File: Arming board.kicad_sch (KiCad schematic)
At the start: 11 parts, among them J2 Conn_01x01_Pin, J3 Conn_01x01_Pin, J4 Conn_01x04_Pin, Q1 SQS141ELNW-T1_GE3

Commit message: Add files via upload
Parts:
- added F2: 50m, Fuse:Fuse_Bourns_TBU-CA, symbol Power_Protection:TBU-CA040-200-WH
- added Q2: SQS141ELNW-T1_GE3, eigene:POWERPAK-1212-8, symbol SQS141ELNW-T1_GE3:SQS141ELNW-T1_GE3
- D2: footprint (none) -> LED_SMD:LED_0603_1608Metric
- DZ1, DZ2, DZ3: footprint (none) -> Diode_SMD:D_SOD-123
- F1: value TBU-CA040-200-WH -> 50m
- J2, J3: footprint (none) -> Connector_PinHeader_1.00mm:PinHeader_1x01_P1.00mm_Horizontal
- J4: footprint (none) -> Connector_PinHeader_1.00mm:PinHeader_1x04_P1.00mm_Horizontal
- R10, R9: value R -> 4.7k; footprint (none) -> Resistor_SMD:R_0805_2012Metric
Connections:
- net BATT_armed: now also Q2.5, Q2.6, Q2.7, Q2.8, Q2.9
- net +BATT renamed Batt+
- net Batt+: now also F2.3, Q2.1, Q2.2, Q2.3
- net Arming logic 1/power_fused renamed Arming logic 1/pwr_fused
- net Disarm renamed Disarm_In_1
- new net Arming logic 2/out: Q2.4
- new net Arming logic 2/pwr_fused: F2.1
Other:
- added sheet Arming logic 2 (Arming logic.kicad_sch)
- sheet Arming logic 1 ports: added arm, disarm, pwr_fused; removed Arm, Disarm, power_fused
- moved on the sheet: D2, DZ1, DZ2, DZ3, R10, R9

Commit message: Add files via upload
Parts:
- removed F2: 50m, Fuse:Fuse_Bourns_TBU-CA, symbol Power_Protection:TBU-CA040-200-WH
- removed J4: Conn_01x04_Pin, Connector_PinHeader_1.00mm:PinHeader_1x04_P1.00mm_Horizontal, symbol Connector:Conn_01x04_Pin
- added D4: 16V, symbol Device:D
- added F2: 50m, symbol Device:Fuse
- added J1: Conn_01x04_Pin, symbol Connector:Conn_01x04_Pin
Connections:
- net Arm_In_1: now also J1.1 (Pin_1)
- net Arming logic 2/pwr_fused: now also F2.2
- net BATT_armed: now also D4.1 (K)
- net Batt+: no longer F1.3, Q1.1, Q1.2, Q1.3, Q2.1, Q2.2, Q2.3
- net Disarm_In_1: now also J1.4 (Pin_4)
- net GND: now also D4.2 (A), J1.2 (Pin_2), J1.3 (Pin_3)
- new net VCC: F1.3, F2.1, Q1.1, Q1.2, Q1.3, Q2.1, Q2.2, Q2.3
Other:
- moved on the sheet: D2, DZ1, DZ2, DZ3, R10, R9

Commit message: Add files via upload
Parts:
- D4: footprint (none) -> Diode_SMD:D_SOD-123
- F2: footprint (none) -> Fuse:Fuse_Bourns_TBU-CA
- J1: footprint (none) -> Connector_PinHeader_1.00mm:PinHeader_1x04_P1.00mm_Horizontal
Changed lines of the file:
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@@
 			)
 		)
-		(property "Footprint" ""
+		(property "Footprint" "Connector_PinHeader_1.00mm:PinHeader_1x04_P1.00mm_Horizontal"
 			(at 41.91 96.52 0)
 			(effects
@@
 			)
 		)
-		(property "Footprint" ""
+		(property "Footprint" "Fuse:Fuse_Bourns_TBU-CA"
 			(at 167.132 34.29 90)
 			(effects
@@
 			)
 		)
-		(property "Footprint" ""
+		(property "Footprint" "Diode_SMD:D_SOD-123"
 			(at 100.33 107.95 0)
 			(effects

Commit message: continued scematic
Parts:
- removed J1: Conn_01x04_Pin, Connector_PinHeader_1.00mm:PinHeader_1x04_P1.00mm_Horizontal, symbol Connector:Conn_01x04_Pin
- removed J2, J3: Conn_01x01_Pin, Connector_PinHeader_1.00mm:PinHeader_1x01_P1.00mm_Horizontal, symbol Connector:Conn_01x01_Pin
- added IC1: CD4043BDR, SOIC127P600X175-16N, symbol rapid_arming:CD4043BDR
- added J1, J11, J4: ~, stigma:Molex_Micro-Fit_3.0_43045-0400_2x02_P3.00mm_Horizontal, symbol Connector_Generic:Conn_02x02_Top_Bottom
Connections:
- net Arm_In_1: no longer DZ1.1 (K)
- net BATT_armed: no longer D4.1 (K), Q1.5, Q1.6, Q1.7, Q1.8, Q1.9, Q2.5, Q2.6, Q2.7, Q2.8, Q2.9
- net GND: now also IC1.8 (VSS), J1.1 (Pin_1), J1.2 (Pin_2), J11.1 (Pin_1), J11.2 (Pin_2), J4.1 (Pin_1), J4.2 (Pin_2)
- net VCC: now also IC1.16 (VDD); no longer Q1.1, Q1.2, Q1.3, Q2.1, Q2.2, Q2.3
- net Arming logic 1/out: no longer names the net of Q1.4
- net Arming logic 1/pwr_fused: no longer names the net of F1.1
- net Arming logic 2/out: no longer names the net of Q2.4
- net Arming logic 2/pwr_fused: no longer names the net of F2.2
- net Batt+ renamed +BATT
- net +BATT: now also Q1.1, Q1.2, Q1.3, Q2.1, Q2.2, Q2.3, J1.3 (Pin_3), J1.4 (Pin_4)
- net Disarm_In_1 renamed disarm
- net disarm: now also IC1.3 (R1), IC1.7 (R2), J11.4 (Pin_4)
- new net +BATT_ARM: D4.1 (K), J4.3 (Pin_3), J4.4 (Pin_4), Q1.5, Q1.6, Q1.7, Q1.8, Q1.9, Q2.5, Q2.6, Q2.7, Q2.8, Q2.9
- new net arm: DZ1.1 (K), IC1.4 (S1), IC1.6 (S2), J11.3 (Pin_3)
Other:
- removed sheet Arming logic 1
- removed sheet Arming logic 2
- note added: "Power In"
- note added: "Power Out"
- note added: "arm/disarm conn."
- moved on the sheet: D2, D4, DZ1, DZ2, DZ3, F1, F2, Q1, Q2, R10, R9

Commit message: continued schematic
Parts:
- removed DZ1, DZ2, DZ3: 16V, Diode_SMD:D_SOD-123, symbol PCM_Diode_Zener_AKL:D_Zener_Generic
- removed F1: 50m, Fuse:Fuse_Bourns_TBU-CA, symbol Power_Protection:TBU-CA040-200-WH
- removed F2: 50m, Fuse:Fuse_Bourns_TBU-CA, symbol Device:Fuse
- removed J11, J4: ~, stigma:Molex_Micro-Fit_3.0_43045-0400_2x02_P3.00mm_Horizontal, symbol Connector_Generic:Conn_02x02_Top_Bottom
- removed Q2: SQS141ELNW-T1_GE3, eigene:POWERPAK-1212-8, symbol SQS141ELNW-T1_GE3:SQS141ELNW-T1_GE3
- added C1, C2: C, Capacitor_SMD:C_0402_1005Metric, symbol Device:C
- added D1, D3, D5: ESD5Zxx, Diode_SMD:D_SOD-523, symbol Diode:ESD5Zxx
- added J2: ~, stigma:Molex_Micro-Fit_3.0_43045-0400_2x02_P3.00mm_Horizontal, symbol Connector_Generic:Conn_02x02_Top_Bottom
- added J3: Conn_02x03_Counter_Clockwise, symbol Connector_Generic:Conn_02x03_Counter_Clockwise
- added R1, R5: 10k, Resistor_SMD:R_0402_1005Metric_Pad0.72x0.64mm_HandSolder, symbol Device:R
- added R2: 1k, symbol Device:R
- added R3, R4: R, Resistor_SMD:R_0402_1005Metric, symbol Device:R
- IC1: LCSC (none) -> C40131
- Q1: Availability In Stock -> (none); Check_prices https://www.snapeda.com/parts/SQS141ELNW-T1/GE3/Vishay/view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 -> (none); Description_1 MOSFET, P-CH/40V/101A/POWERPAK 1212-8SLW ROHS COMPLIANT: YES -> 55℃~+175℃ 1 P-Channel 10mΩ@10V 119W 141nC@10V 2V 347pF 40V 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; LCSC (none) -> C6818689; MP SQS141ELNW-T1/GE3 -> (none); Package None -> (none); Price None -> (none); SnapEDA_Link https://www.snapeda.com/parts/SQS141ELNW-T1/GE3/Vishay/view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 -> (none)
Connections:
- net +BATT: now also D5.1 (K)
- net +BATT_ARM: now also J2.3 (Pin_3), J2.4 (Pin_4)
- net GND: now also C1.2, C2.2, D1.2 (A), D3.2 (A), D5.2 (A), J2.1 (Pin_1), J2.2 (Pin_2), J3.1 (Pin_1)
- net VCC: now also J3.6 (Pin_6), R1.2, R5.2
- net arm: now also IC1.7 (R2), C1.1, R3.2; no longer IC1.4 (S1), IC1.6 (S2)
- net disarm: now also IC1.6 (S2), C2.1, R4.2; no longer IC1.3 (R1), IC1.7 (R2)
- net at Q1.4: now also R1.1, R2.2
- net at IC1.5 (ENABLE): now also R5.1
- net at IC1.9 (Q2): now also R2.1
- new net: D3.1 (K), J3.4 (Pin_4), R4.1
- new net: D1.1 (K), J3.5 (Pin_5), R3.1
- no-connect marks 0 -> 9
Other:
- note added: "flyback"
- note added: "gate current limit resistor?"
- moved on the sheet: D2, D4, IC1, Q1, R10, R9

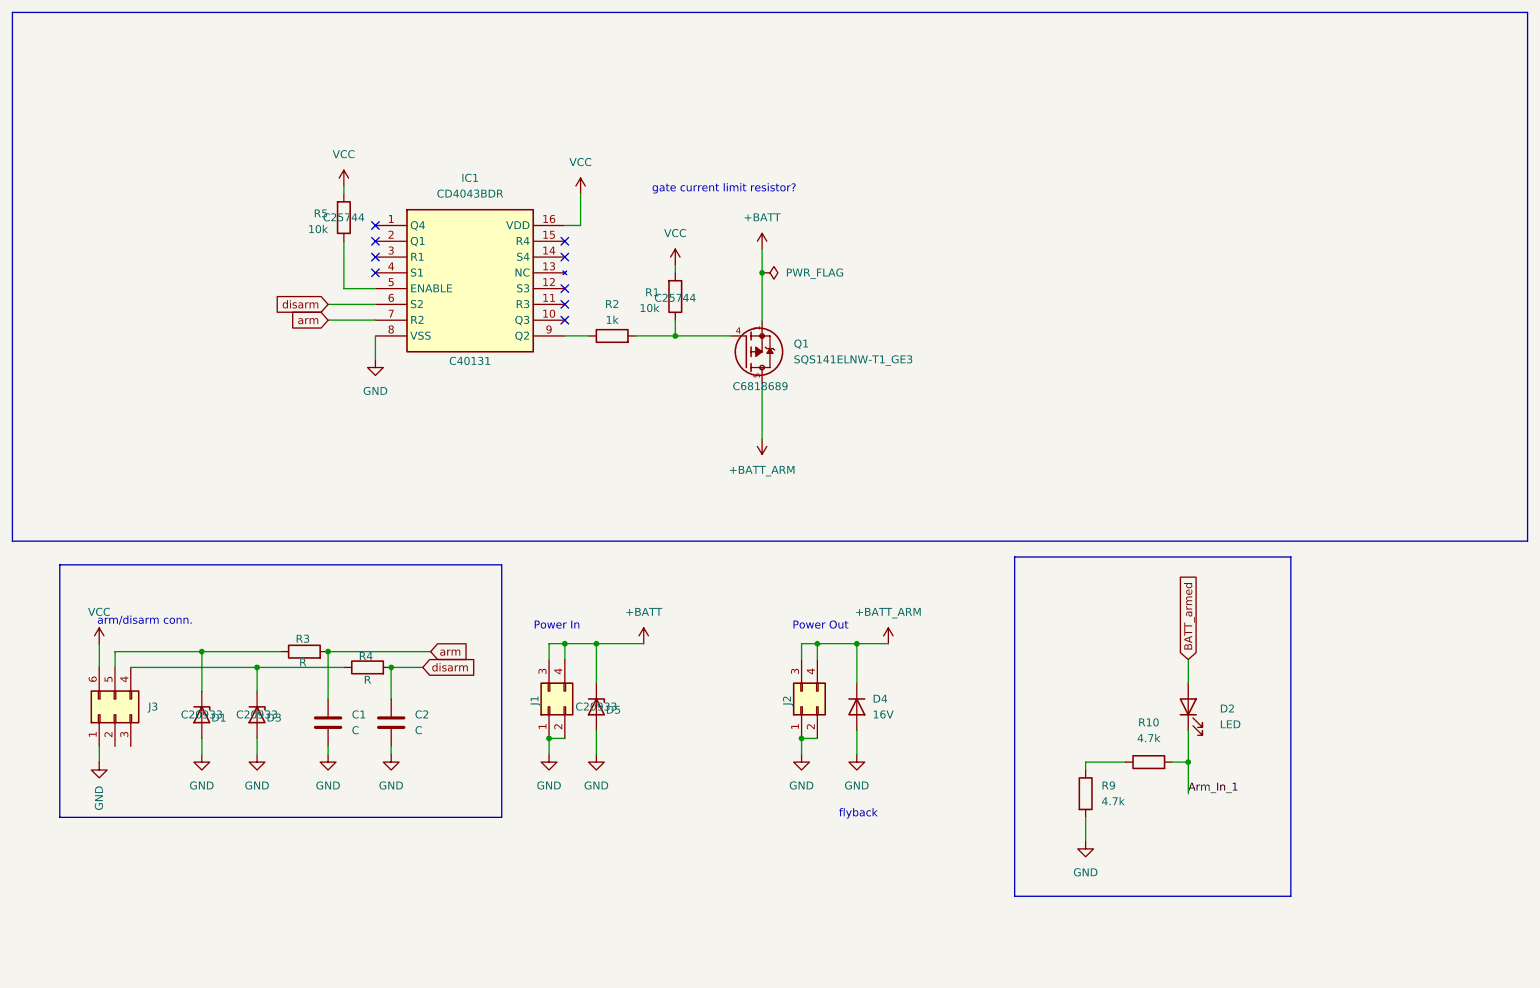
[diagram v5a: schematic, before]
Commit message: finished first scematic draft
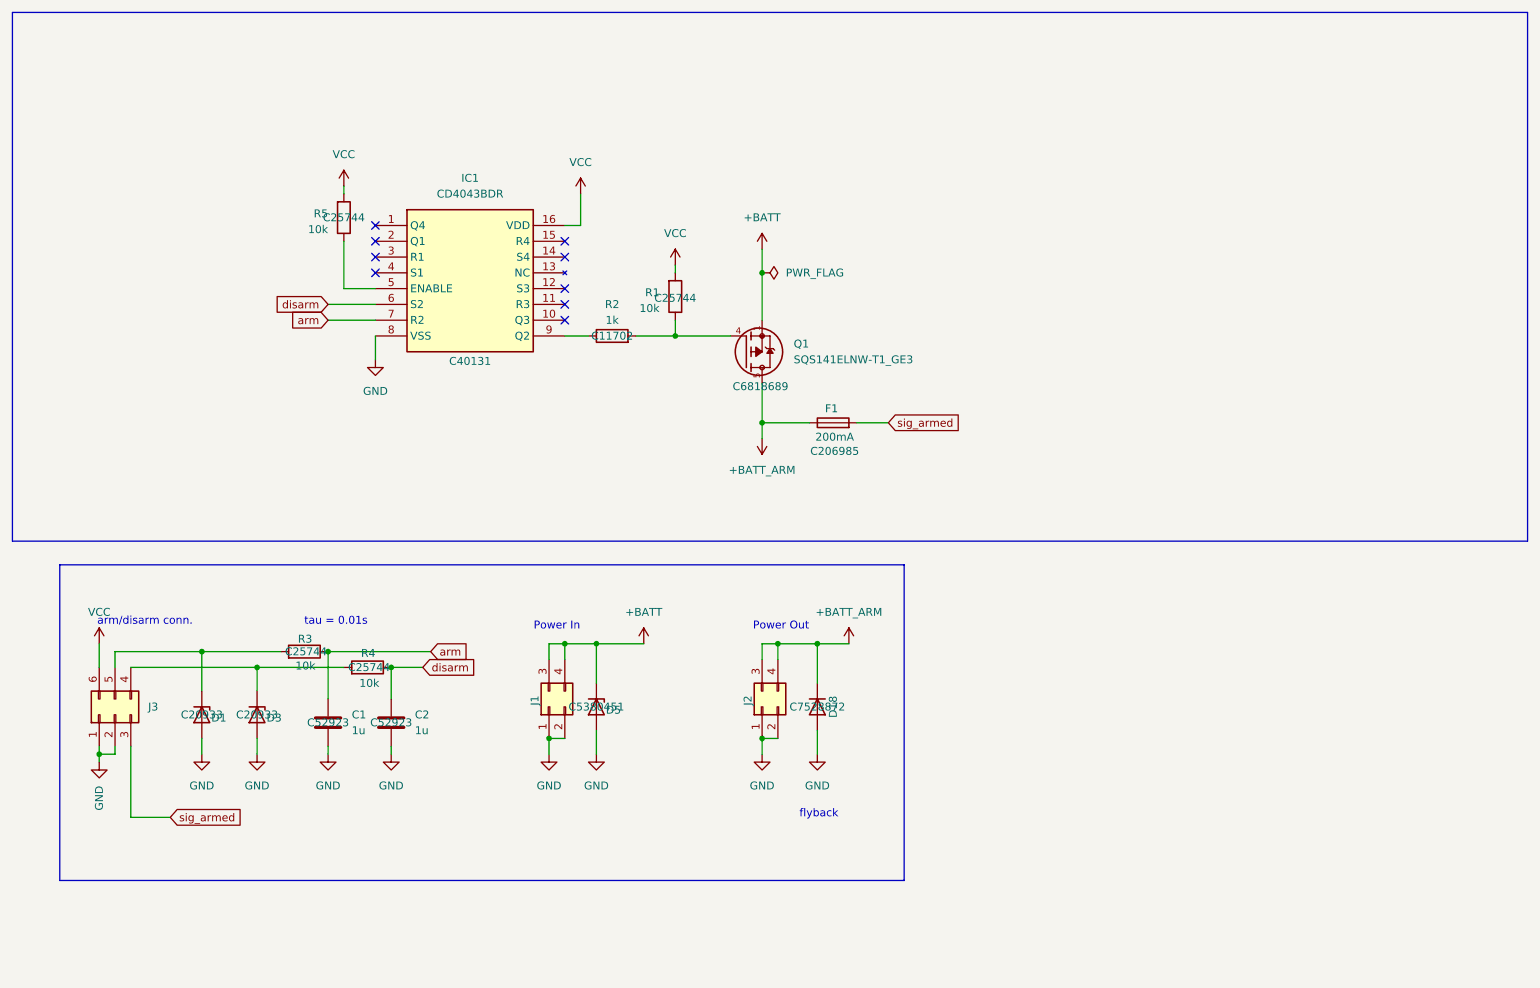
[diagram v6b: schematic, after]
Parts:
- removed D2: LED, LED_SMD:LED_0603_1608Metric, symbol Device:LED
- removed D4: 16V, Diode_SMD:D_SOD-123, symbol Device:D
- removed R10, R9: 4.7k, Resistor_SMD:R_0805_2012Metric, symbol Device:R
- added D18: D, Diode_SMD:D_SOD-323_HandSoldering, symbol Device:D
- added F1: 200mA, Fuse:Fuse_1206_3216Metric_Pad1.42x1.75mm_HandSolder, symbol Device:Fuse
- C1, C2: value C -> 1u; LCSC (none) -> C52923
- D5: value ESD5Zxx -> TS1811LD-CX; LCSC C20933 -> C5380451
- J1, J2: footprint stigma:Molex_Micro-Fit_3.0_43045-0400_2x02_P3.00mm_Horizontal -> Connector_Molex:Molex_Micro-Fit_3.0_43045-0400_2x02_P3.00mm_Horizontal
- J3: footprint (none) -> Connector_Molex:Molex_Micro-Fit_3.0_43045-0600_2x03_P3.00mm_Horizontal
- Q1: footprint eigene:POWERPAK-1212-8 -> rapid_arming:POWERPAK-1212-8
- R2: footprint (none) -> Resistor_SMD:R_0402_1005Metric_Pad0.72x0.64mm_HandSolder; LCSC (none) -> C11702
- R3, R4: value R -> 10k; footprint Resistor_SMD:R_0402_1005Metric -> Resistor_SMD:R_0402_1005Metric_Pad0.72x0.64mm_HandSolder; LCSC (none) -> C25744
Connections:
- net +BATT_ARM: now also D18.1 (K), F1.1
- net GND: now also J3.2 (Pin_2), D18.2 (A)
- net arm: now also R3.1; no longer R3.2
- net disarm: now also R4.1; no longer R4.2
- net sig_armed: now reaches J3.3 (Pin_3)
- net sig_armed: now also F1.2
- net at D3.1 (K), J3.4 (Pin_4): now also R4.2; no longer R4.1
- net at D1.1 (K), J3.5 (Pin_5): now also R3.2; no longer R3.1
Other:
- note added: "tau = 0.01s"
- note removed: "gate current limit resistor?"
- moved on the sheet: J2

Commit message: Replaced 6-Pin with 4-Pin connector, added input pulldown
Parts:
- removed F1: 200mA, Fuse:Fuse_1206_3216Metric_Pad1.42x1.75mm_HandSolder, symbol Device:Fuse
- removed J3: Conn_02x03_Counter_Clockwise, Connector_Molex:Molex_Micro-Fit_3.0_43045-0600_2x03_P3.00mm_Horizontal, symbol Connector_Generic:Conn_02x03_Counter_Clockwise
- added D19: D, Diode_SMD:D_SOD-323_HandSoldering, symbol Device:D
- added D6: TS1811LD-CX, Diode_SMD:D_SOD-523, symbol Diode:ESD5Zxx
- added J4, J5, J6: (no value), Connector_Molex:Molex_Micro-Fit_3.0_43045-0400_2x02_P3.00mm_Horizontal, symbol Connector_Generic:Conn_02x02_Top_Bottom
- added R6, R7: 10k, Resistor_SMD:R_0402_1005Metric_Pad0.72x0.64mm_HandSolder, symbol Device:R
- IC1: footprint SOIC127P600X175-16N -> Package_SO:SOIC-16W_7.5x10.3mm_P1.27mm
- J1, J2: value ~ -> (none)
- Q1: footprint rapid_arming:POWERPAK-1212-8 -> Package_SO:PowerPAK_SO-8_Single
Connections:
- net +BATT: now also D6.1 (K), J4.3 (Pin_3), J4.4 (Pin_4)
- net +BATT_ARM: now also D19.1 (K), J5.3 (Pin_3), J5.4 (Pin_4)
- net GND: now also D19.2 (A), D6.2 (A), J4.1 (Pin_1), J4.2 (Pin_2), J5.1 (Pin_1), J5.2 (Pin_2), J6.1 (Pin_1), R6.1, R7.1
- net VCC: now also J6.2 (Pin_2)
- net arm: now also R6.2
- net disarm: now also R7.2
- net at D3.1 (K), R4.2: now also J6.4 (Pin_4)
- net at D1.1 (K), R3.2: now also J6.3 (Pin_3)

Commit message: Replaced connector with molex, fixed mosfet footprint
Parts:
- removed J6: (no value), Connector_Molex:Molex_Micro-Fit_3.0_43045-0400_2x02_P3.00mm_Horizontal, symbol Connector_Generic:Conn_02x02_Top_Bottom
- added J3: Conn_01x04, Connector_Molex:Molex_Micro-Fit_3.0_43650-0400_1x04_P3.00mm_Horizontal, symbol Connector_Generic:Conn_01x04
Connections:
- net +BATT_ARM: no longer Q1.6, Q1.7, Q1.8, Q1.9
- net GND: now also J3.1 (Pin_1)
- net VCC: now also J3.4 (Pin_4)
- net at D3.1 (K), R4.2: now also J3.2 (Pin_2)
- net at D1.1 (K), R3.2: now also J3.3 (Pin_3)
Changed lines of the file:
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@@
 	(wire
 		(pts
-			(xy 34.29 120.65) (xy 54.61 120.65)
-		)
-		(stroke
-			(width 0)
-			(type default)
-		)
-	)
-	(wire
-		(pts
 			(xy 106.68 44.45) (xy 106.68 49.53)
 		)
@@
 	(wire
 		(pts
+			(xy 45.72 118.11) (xy 31.75 118.11)
+		)
+		(stroke
+			(width 0)
+			(type default)
+		)
+	)
+	(wire
+		(pts
 			(xy 73.66 69.85) (xy 73.66 72.39)
 		)
@@
 	(wire
 		(pts
-			(xy 31.75 118.11) (xy 31.75 120.65)
+			(xy 34.29 120.65) (xy 34.29 127)
 		)
 		(stroke
@@
 	(wire
 		(pts
-			(xy 49.53 62.23) (xy 68.58 62.23)
+			(xy 54.61 120.65) (xy 34.29 120.65)
 		)
 		(stroke
@@
 	(wire
 		(pts
-			(xy 46.99 64.77) (xy 59.69 64.77)
+			(xy 49.53 62.23) (xy 68.58 62.23)
 		)
 		(stroke
@@
 	(wire
 		(pts
-			(xy 45.72 118.11) (xy 45.72 124.46)
+			(xy 46.99 64.77) (xy 59.69 64.77)
 		)
 		(stroke
@@
 	(wire
 		(pts
-			(xy 54.61 120.65) (xy 54.61 124.46)
+			(xy 45.72 118.11) (xy 45.72 124.46)
 		)
 		(stroke
@@
 	(wire
 		(pts
-			(xy 66.04 134.62) (xy 66.04 133.35)
+			(xy 54.61 120.65) (xy 54.61 124.46)
 		)
 		(stroke
@@
 	(wire
 		(pts
-			(xy 31.75 118.11) (xy 45.72 118.11)
+			(xy 66.04 134.62) (xy 66.04 133.35)
 		)
 		(stroke
@@
 	(wire
 		(pts
+			(xy 31.75 118.11) (xy 31.75 127)
+		)
+		(stroke
+			(width 0)
+			(type default)
+		)
+	)
+	(wire
+		(pts
 			(xy 135.89 132.08) (xy 138.43 132.08)
 		)
@@
 	(wire
 		(pts
-			(xy 31.75 133.35) (xy 31.75 137.16)
-		)
-		(stroke
-			(width 0)
-			(type default)
-		)
-	)
-	(wire
-		(pts
-			(xy 34.29 133.35) (xy 34.29 137.16)
+			(xy 29.21 127) (xy 29.21 123.19)
 		)
 		(stroke
@@
 		(pin "5"
 		)
-		(pin "8"
+		(pin "5"
 		)
 		(pin "2"
@@
 		(pin "4"
 		)
-		(pin "6"
+		(pin "5"
 		)
 		(pin "3"
@@
 		(pin "1"
 		)
-		(pin "7"
+		(pin "5"
 		)
-		(pin "9"
+		(pin "5"
 		)
 		(instances
@@
 	(symbol
 		(lib_id "power:GND")
-		(at 31.75 137.16 0)
+		(at 36.83 127 180)
 		(unit 1)
 		(body_style 1)
@@
 		(in_pos_files yes)
 		(dnp no)
-		(fields_autoplaced yes)
 		(property "Reference" "#PWR012"
-			(at 31.75 143.51 0)
+			(at 36.83 120.65 0)
 			(hide yes)
 			(show_name no)
@@
 		)
 		(property "Value" "GND"
-			(at 31.7501 140.97 90)
+			(at 39.37 127.254 90)
 			(show_name no)
 			(do_not_autoplace no)
@@
 		)
 		(property "Footprint" ""
-			(at 31.75 137.16 0)
+			(at 36.83 127 0)
 			(hide yes)
 			(show_name no)
@@
 		)
 		(property "Datasheet" ""
-			(at 31.75 137.16 0)
+			(at 36.83 127 0)
 			(hide yes)
 			(show_name no)
@@
 		)
 		(property "Description" "Power symbol creates a global label with name \"GND\" , ground"
-			(at 31.75 137.16 0)
+			(at 36.83 127 0)
 			(hide yes)
 			(show_name no)
@@
 	(symbol
 		(lib_id "power:VCC")
-		(at 34.29 137.16 180)
+		(at 29.21 123.19 0)
 		(unit 1)
 		(body_style 1)
@@
 		(fields_autoplaced yes)
 		(property "Reference" "#PWR06"
-			(at 34.29 133.35 0)
+			(at 29.21 127 0)
 			(hide yes)
 			(show_name no)
@@
 		)
 		(property "Value" "VCC"
-			(at 34.29 142.24 0)
+			(at 29.21 118.11 0)
 			(show_name no)
 			(do_not_autoplace no)
@@
 		)
 		(property "Footprint" ""
-			(at 34.29 137.16 0)
+			(at 29.21 123.19 0)
 			(hide yes)
 			(show_name no)
@@
 		)
 		(property "Datasheet" ""
-			(at 34.29 137.16 0)
+			(at 29.21 123.19 0)
 			(hide yes)
 			(show_name no)
@@
 		)
 		(property "Description" "Power symbol creates a global label with name \"VCC\""
-			(at 34.29 137.16 0)
+			(at 29.21 123.19 0)
 			(hide yes)
 			(show_name no)
@@
 	)
 	(symbol
+		(lib_id "Connector_Generic:Conn_01x04")
+		(at 34.29 132.08 270)
+		(unit 1)
+		(body_style 1)
+		(exclude_from_sim no)
+		(in_bom yes)
+		(on_board yes)
+		(in_pos_files yes)
+		(dnp no)
+		(fields_autoplaced yes)
+		(property "Reference" "J3"
+			(at 33.02 135.89 90)
+			(show_name no)
+			(do_not_autoplace no)
+			(effects
+				(font
+					(size 1.27 1.27)
+				)
+			)
+		)
+		(property "Value" "Conn_01x04"
+			(at 33.02 138.43 90)
+			(show_name no)
+			(do_not_autoplace no)
+			(effects
+				(font
+					(size 1.27 1.27)
+				)
+			)
+		)
+		(property "Footprint" "Connector_Molex:Molex_Micro-Fit_3.0_43650-0400_1x04_P3.00mm_Horizontal"
+			(at 34.29 132.08 0)
+			(hide yes)
+			(show_name no)
+			(do_not_autoplace no)
+			(effects
+				(font
+					(size 1.27 1.27)
+				)
+			)
+		)
+		(property "Datasheet" ""
+			(at 34.29 132.08 0)
+			(hide yes)
+			(show_name no)
+			(do_not_autoplace no)
+			(effects
+				(font
+					(size 1.27 1.27)
+				)
+			)
+		)
+		(property "Description" "Generic connector, single row, 01x04, script generated (kicad-library-utils/schlib/autogen/connector/)"
+			(at 34.29 132.08 0)
+			(hide yes)
+			(show_name no)
+			(do_not_autoplace no)
+			(effects
+				(font
+					(size 1.27 1.27)
+				)
+			)
+		)
+		(pin "4"
+		)
+		(pin "2"
+		)
+		(pin "1"
+		)
+		(pin "3"
+		)
+		(instances
+			(project "Arming board"
+				(path "/a8577761-41ea-4572-892c-e689011487d6"
+					(reference "J3")
+					(unit 1)
+				)
+			)
+		)
+	)
+	(symbol
 		(lib_id "Device:C")
 		(at 76.2 129.54 0)
@@
 					(unit 1)
 				)
-			)
-		)
-	)
-	(symbol
-		(lib_id "Connector_Generic:Conn_02x02_Top_Bottom")
-		(at 31.75 128.27 90)
-		(unit 1)
-		(body_style 1)
-		(exclude_from_sim no)
-		(in_bom yes)
-		(on_board yes)
-		(in_pos_files yes)
-		(dnp no)
-		(property "Reference" "J6"
-			(at 29.464 127.254 0)
-			(show_name no)
-			(do_not_autoplace no)
-			(effects
-				(font
-					(size 1.27 1.27)
-				)
-			)
-		)
-		(property "Value" ""
-			(at 28.194 128.524 0)
-			(hide yes)
-			(show_name no)
-			(do_not_autoplace no)
-			(effects
-				(font
-					(size 1.27 1.27)
-				)
-			)
-		)
-		(property "Footprint" "Connector_Molex:Molex_Micro-Fit_3.0_43045-0400_2x02_P3.00mm_Horizontal"
-			(at 31.75 128.27 0)
-			(hide yes)
-			(show_name no)
-			(do_not_autoplace no)
-			(effects
-				(font
-					(size 1.27 1.27)
-				)
-			)
-		)
-		(property "Datasheet" "https://www.mouser.de/ProductDetail/Molex/43045-0400?qs=UeCeOHRHQeaIqmxE9Bxdrw%3D%3D#:~:text=Datenblatt%3A,43045%2D0400%20Datenblatt"
-			(at 31.75 128.27 0)
-			(hide yes)
-			(show_name no)
-			(do_not_autoplace no)
-			(effects
-				(font
-					(size 1.27 1.27)
-				)
-			)
-		)
-		(property "Description" "43045-0400"
-			(at 31.75 128.27 0)
-			(hide yes)
-			(show_name no)
-			(do_not_autoplace no)
-			(effects
-				(font
-					(size 1.27 1.27)
-				)
-			)
-		)
-		(property "LCSC#" "x"
-			(at 31.75 128.27 0)
-			(hide yes)
-			(show_name no)
-			(do_not_autoplace no)
-			(effects
-				(font
-					(size 1.27 1.27)
-				)
-			)
-		)
-		(pin "3"
-		)
-		(pin "2"
-		)
-		(pin "4"
-		)
-		(pin "1"
-		)
-		(instances
-			(project "Arming board"
-				(path "/a8577761-41ea-4572-892c-e689011487d6"
-					(reference "J6")
-					(unit 1)
-				)
